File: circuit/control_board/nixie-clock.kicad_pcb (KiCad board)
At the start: 2 copper layers, 42 parts, among them IC1 ATMEGA328-P, P1 CONN_2, P2 CONN_2, P3 CONN_4, P4 CONN_4, P5 CONN_8, P6 CONN_12, P7 CONN_2, P8 CONN_2, Q1 NPN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

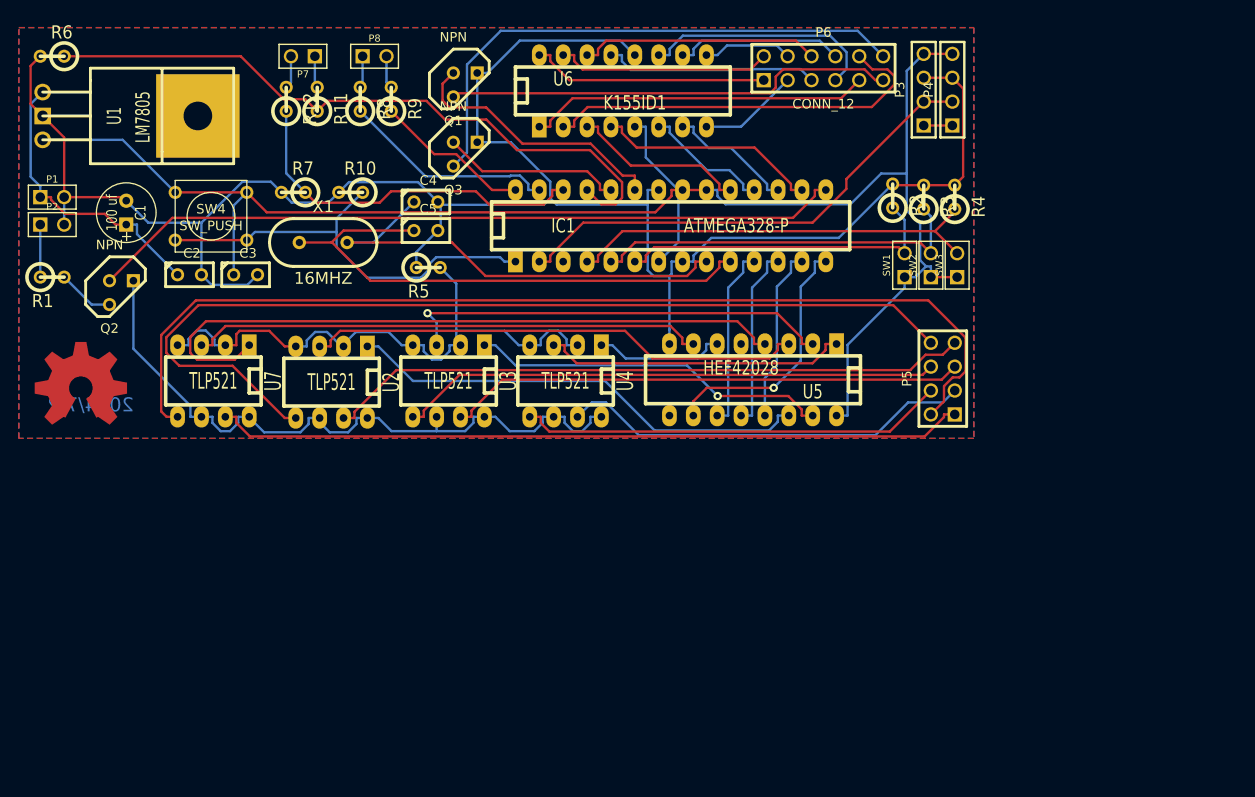
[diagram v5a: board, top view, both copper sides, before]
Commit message: Control Board: Rearrange the position of the PCB board
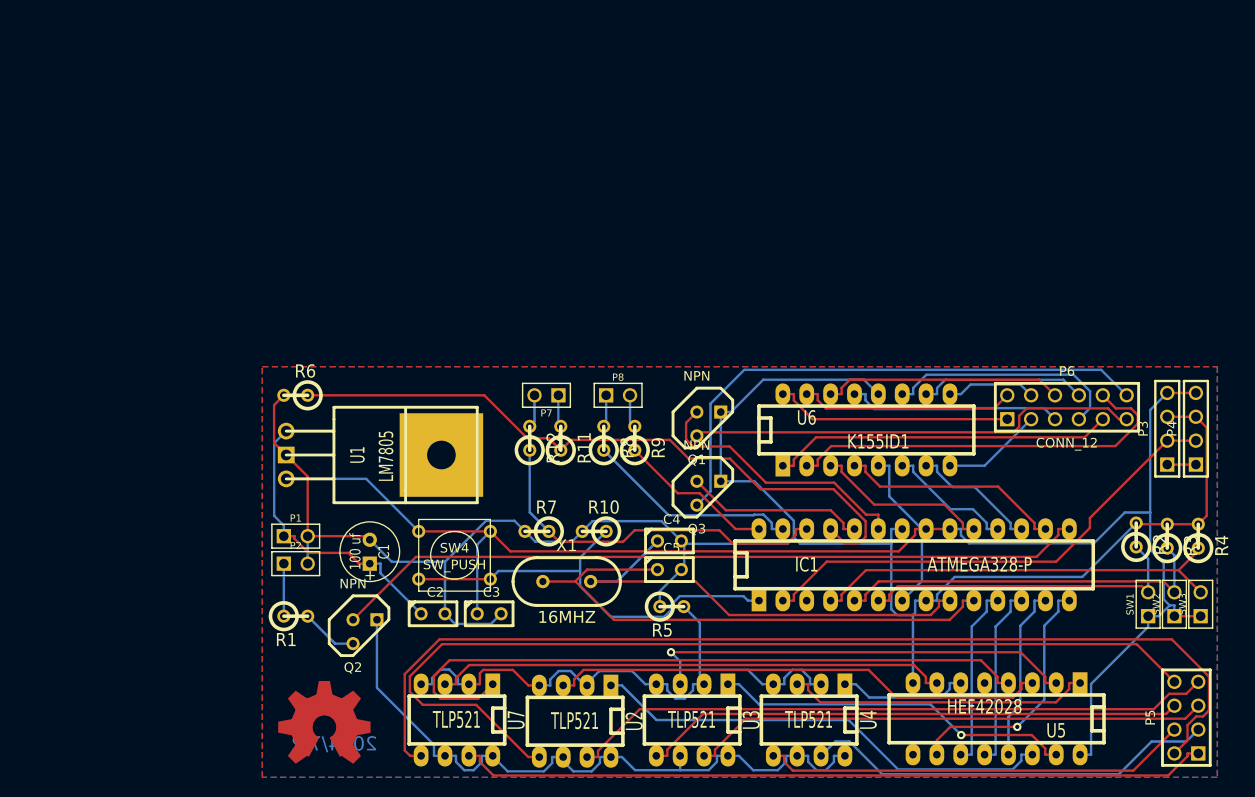
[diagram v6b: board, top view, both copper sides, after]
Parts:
- moved R2 44.4 mm to (192.5, 98.9)
- moved R3 44.4 mm to (195.8, 99.1)
- moved SW2 44.4 mm to (196.6, 106.3)
- moved U6 44.4 mm to (163.8, 87.8)
- moved P3 44.4 mm to (195.8, 87.6)
- moved P4 44.4 mm to (198.9, 87.6)
- moved P5 44.4 mm to (197.9, 118.4)
- moved P7 44.4 mm to (129.8, 84.1)
- moved R11 44.4 mm to (131.3, 88.6)
- moved SW1 44.4 mm to (193.8, 106.3)
- moved SW3 44.4 mm to (199.4, 106.3)
- moved U2 44.4 mm to (132.8, 118.7)
- moved U3 44.4 mm to (145.3, 118.6)
- moved U4 44.4 mm to (157.7, 118.6)
- moved U5 44.4 mm to (177.7, 118.5)
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
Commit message: Control board: Add two 2*1 pin array for 5v power
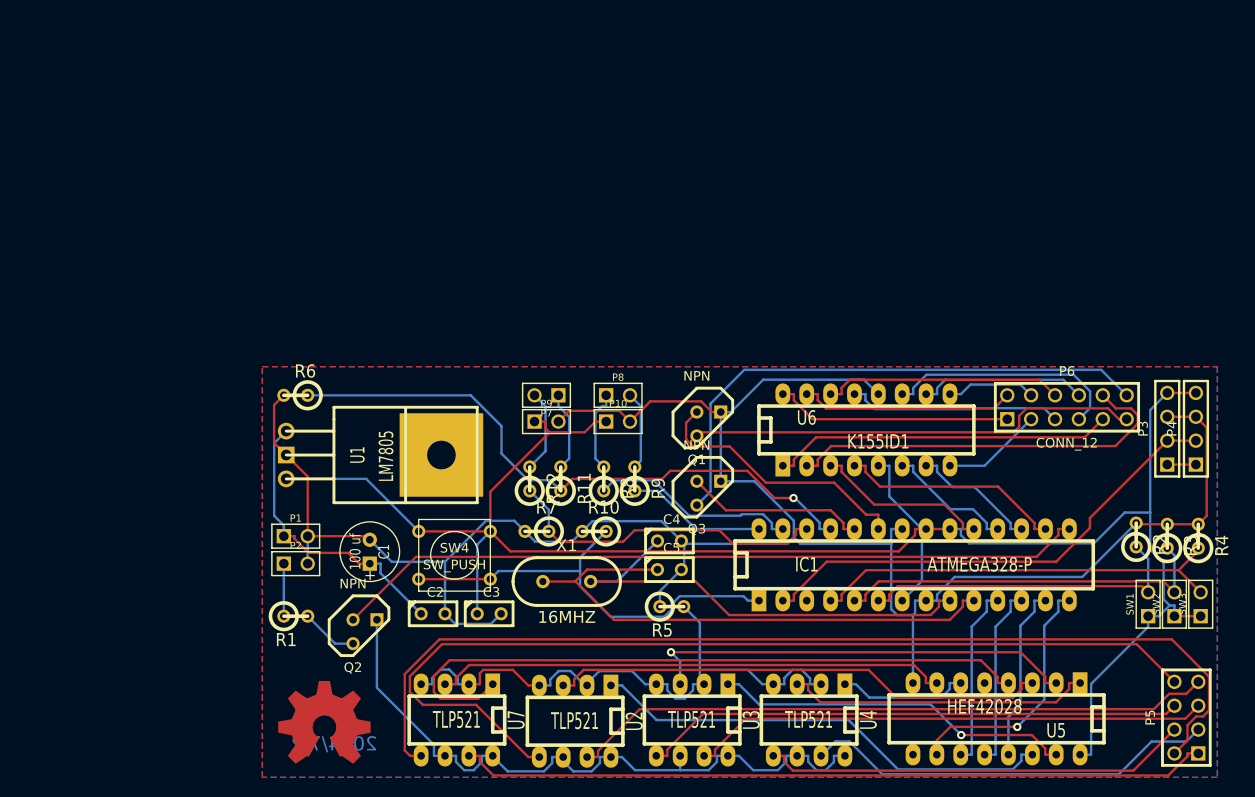
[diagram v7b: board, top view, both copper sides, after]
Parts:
- added P10: CONN_2, PIN_ARRAY_2X1, F.Cu at (137.4, 86.9)
- added P9: CONN_2, PIN_ARRAY_2X1, F.Cu at (129.8, 86.9)
- moved R11 4.32 mm to (131.3, 93.0)
- moved R12 4.32 mm to (128.0, 93.0)
- moved R8 4.32 mm to (135.9, 93.0)
- moved R9 4.32 mm to (139.2, 93.0)
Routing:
- net 5V: track 179.3 -> 201.4 mm
- net GND: track 216.3 -> 235.9 mm
- net MP3 Tx: track 72.1 -> 65.4 mm, vias 0 -> 1
- net N-0000022: track 3.41 -> 8.71 mm
- net N-0000041: track 3.51 -> 8.80 mm
- net N-0000042: track 3.41 -> 8.46 mm
- net N-0000023: track 3.51 -> 8.36 mm
- net MP3 Rx: track 39.5 -> 35.1 mm
- net I2C SCL: track 16.7 -> 14.9 mm
- net I2C SDA: track 23.0 -> 22.2 mm

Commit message: Control board: Add the board edge
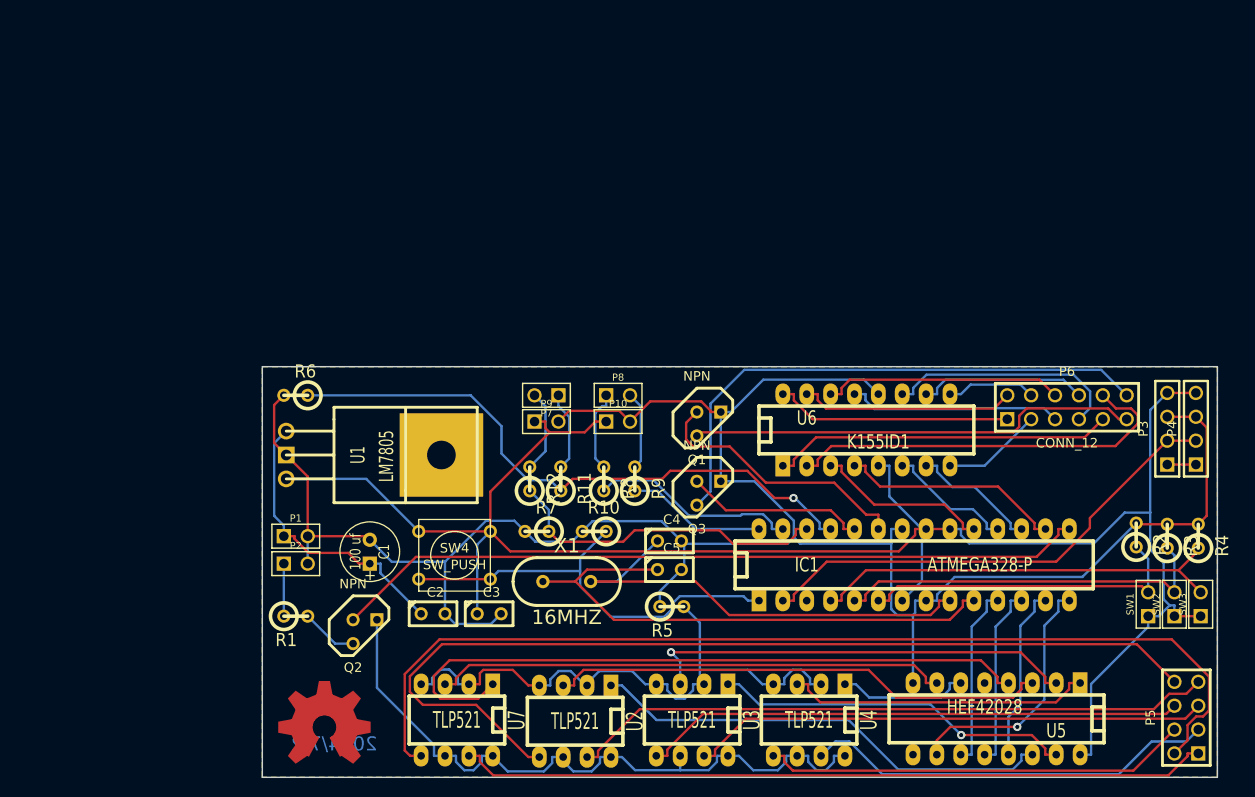
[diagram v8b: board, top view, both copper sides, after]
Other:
- board outline added: 101.6 x 43.7 mm
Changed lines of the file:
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@@
-(kicad_pcb (version 3) (host pcbnew "(2013-mar-13)-testing")
+(kicad_pcb (version 3) (host pcbnew "(2013-jul-07)-stable")
   (general
     (links 125)
     (no_connects 0)
-    (area 92.218934 80.4799 202.7301 124.714001)
+    (area 92.218934 80.4799 202.7301 124.789001)
     (thickness 1.6)
-    (drawings 1)
+    (drawings 5)
     (tracks 593)
     (zones 0)
@@
     (autoplace_cost180 10)
     (fp_text reference X1 (at 0 -3.81) (layer F.SilkS)
-      (effects (font (thickness 0.3048)))
+      (effects (font (size 1.524 1.524) (thickness 0.3048)))
     )
     (fp_text value 16MHZ (at 0 3.81) (layer F.SilkS)
-      (effects (font (thickness 0.3048)))
+      (effects (font (size 1.524 1.524) (thickness 0.3048)))
     )
     (fp_line (start -3.175 2.54) (end 3.175 2.54) (layer F.SilkS) (width 0.3175))
@@
     (at 106.172 119.38)
     (fp_text reference OSHW_COPPER_10MM (at 0 0) (layer F.SilkS) hide
-      (effects (font (thickness 0.3048)))
+      (effects (font (size 1.524 1.524) (thickness 0.3048)))
     )
     (fp_text value VAL** (at 0 0) (layer F.SilkS) hide
-      (effects (font (thickness 0.3048)))
+      (effects (font (size 1.524 1.524) (thickness 0.3048)))
     )
     (pad "" smd trapezoid (at 0 -4.1656 180) (size 1.45796 1.4986) (rect_delta 0 -0.2794 )
@@
     )
   )
+  (gr_line (start 99.568 124.714) (end 201.168 124.714) (angle 90) (layer Edge.Cuts) (width 0.15))
+  (gr_line (start 99.568 81.026) (end 99.568 124.714) (angle 90) (layer Edge.Cuts) (width 0.15))
+  (gr_line (start 201.168 81.026) (end 99.568 81.026) (angle 90) (layer Edge.Cuts) (width 0.15))
+  (gr_line (start 201.168 124.714) (end 201.168 81.026) (angle 90) (layer Edge.Cuts) (width 0.15))
   (gr_text 2014/7/2 (at 107.188 121.158) (layer B.Cu)
     (effects (font (size 1.5 1.5) (thickness 0.3)) (justify mirror))
